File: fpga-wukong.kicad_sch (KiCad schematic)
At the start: 2 parts, among them J4 QMTECH FPGA Module U4, J5 QMTECH FPGA Module U5

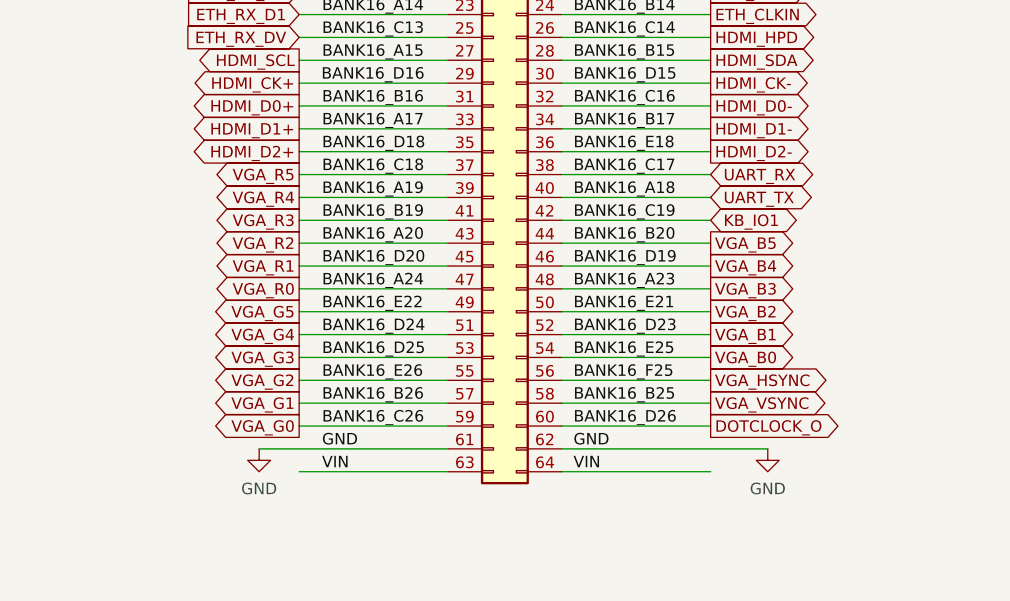
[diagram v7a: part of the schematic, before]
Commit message: finish routing VGA connector
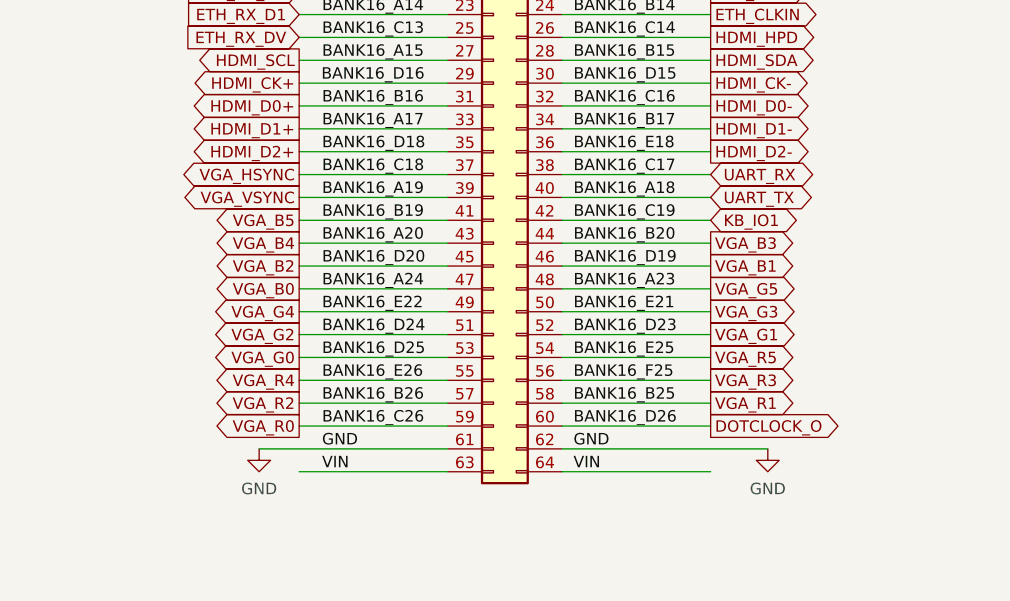
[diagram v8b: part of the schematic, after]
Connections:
- net VGA_B0: now also J4.47 (Pin_47); no longer J4.54 (Pin_54)
- net VGA_B1: now also J4.46 (Pin_46); no longer J4.52 (Pin_52)
- net VGA_B2: now also J4.45 (Pin_45); no longer J4.50 (Pin_50)
- net VGA_B3: now also J4.44 (Pin_44); no longer J4.48 (Pin_48)
- net VGA_B4: now also J4.43 (Pin_43); no longer J4.46 (Pin_46)
- net VGA_B5: now also J4.41 (Pin_41); no longer J4.44 (Pin_44)
- net VGA_G0: now also J4.53 (Pin_53); no longer J4.59 (Pin_59)
- net VGA_G1: now also J4.52 (Pin_52); no longer J4.57 (Pin_57)
- net VGA_G2: now also J4.51 (Pin_51); no longer J4.55 (Pin_55)
- net VGA_G3: now also J4.50 (Pin_50); no longer J4.53 (Pin_53)
- net VGA_G4: now also J4.49 (Pin_49); no longer J4.51 (Pin_51)
- net VGA_G5: now also J4.48 (Pin_48); no longer J4.49 (Pin_49)
- net VGA_HSYNC: now also J4.37 (Pin_37); no longer J4.56 (Pin_56)
- net VGA_R0: now also J4.59 (Pin_59); no longer J4.47 (Pin_47)
- net VGA_R1: now also J4.58 (Pin_58); no longer J4.45 (Pin_45)
- net VGA_R2: now also J4.57 (Pin_57); no longer J4.43 (Pin_43)
- net VGA_R3: now also J4.56 (Pin_56); no longer J4.41 (Pin_41)
- net VGA_R4: now also J4.55 (Pin_55); no longer J4.39 (Pin_39)
- net VGA_R5: now also J4.54 (Pin_54); no longer J4.37 (Pin_37)
- net VGA_VSYNC: now also J4.39 (Pin_39); no longer J4.58 (Pin_58)
